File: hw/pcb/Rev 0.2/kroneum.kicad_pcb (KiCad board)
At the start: 2 copper layers, 57.6 x 68.4 mm, 18 parts, among them J1 USB_B_Micro, J2 SWD_I2C_BOOT, SW1 Boot_Mode_Btn, SW2 Ctrl_One_Btn, SW3 Reset_Btn, SW4 Ctrl_Ten_Btn, U1 STM32F042F4Px

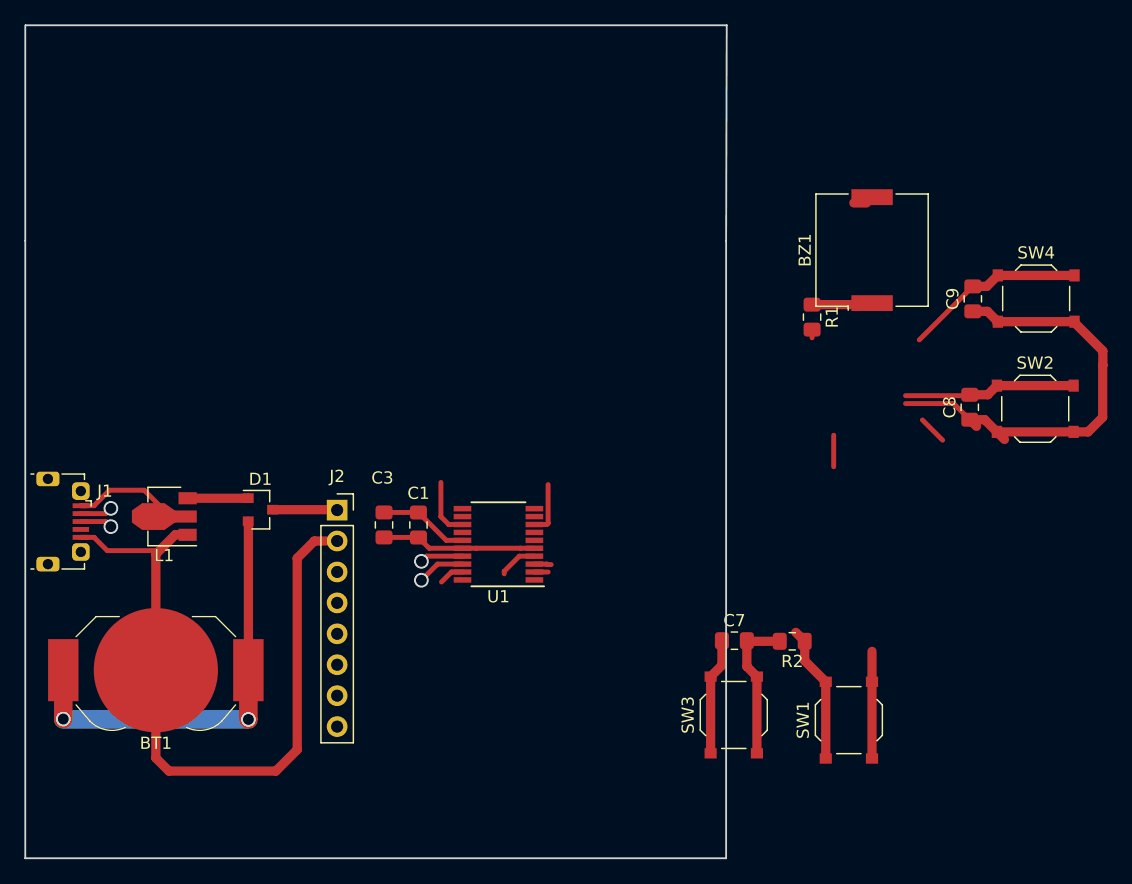
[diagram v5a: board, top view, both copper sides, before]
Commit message: hw: first PCB version with all nets connected.
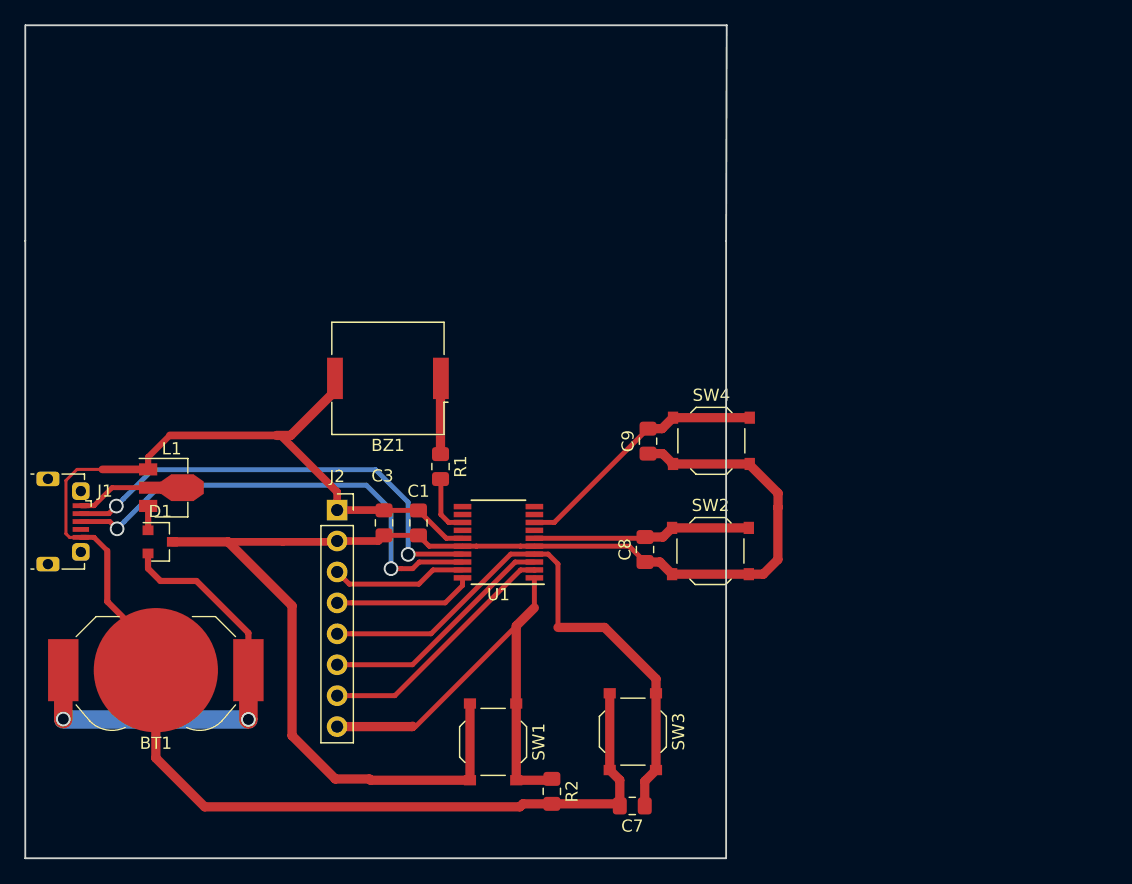
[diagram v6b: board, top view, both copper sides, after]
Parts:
- moved BZ1 41.1 mm to (151.1, 93.6), turned to 180 degrees
- moved R1 32.9 mm to (155.4, 100.8)
- moved SW1 29.3 mm to (159.8, 123.4), turned to 270 degrees
- moved SW4 29.1 mm to (177.7, 98.7)
- moved C8 29.1 mm to (172.2, 107.6)
- moved C9 29.1 mm to (172.5, 98.7)
- moved SW2 29.1 mm to (177.6, 107.8)
- moved R2 23.3 mm to (164.6, 127.5), turned to 270 degrees
- moved C7 16.0 mm to (171.2, 128.7), turned to 180 degrees
- moved D1 8.64 mm to (132.4, 107.0)
- moved SW3 8.40 mm to (171.2, 122.6), turned to 270 degrees
- moved L1 2.39 mm to (132.9, 102.6), turned to 0 degrees
- moved C1 0.17 mm to (153.6, 105.5)
- moved C3 0.17 mm to (150.8, 105.5)
- moved U1 0.17 mm to (160.2, 107.0)
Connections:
- J2 pad 1: VDD -> GND
- J2 pad 2: GND -> VDD
- J2 pad 3: SCL -> SWDIO
- J2 pad 4: SDA -> SWCLK
- J2 pad 5: BOOT0 -> NRST
- J2 pad 6: NRST -> SCL
- J2 pad 7: SWCLK -> SDA
- J2 pad 8: SWDIO -> BOOT0
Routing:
- net VDD: track 63.8 -> 114.5 mm
- net GND: track 79.6 -> 123.6 mm
- net NRST: track 13.0 -> 47.2 mm
- net USB_D+: track 6.57 -> 39.0 mm
- net USB_D-: track 6.20 -> 38.2 mm
- net BOOT0: track 11.4 -> 40.2 mm
- net SDA: track 1.27 -> 20.6 mm
- net SCL: track 3.75 -> 19.7 mm
- net SWDIO: track 2.07 -> 11.2 mm
- net SWCLK: track 2.58 -> 11.5 mm
- net Ctrl_One: track 14.1 -> 18.1 mm
- net Net-(D1-Pad1): track 4.98 -> 2.00 mm
- net Net-(BT1-Pad1): track 35.5 -> 38.0 mm
- net USB_VBUS: track 13.8 -> 11.3 mm
- net Ctrl_Ten: track 19.3 -> 21.2 mm
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
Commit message: hw: semi final PCB versions.
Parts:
- moved C7 34.0 mm to (137.2, 127.0), turned to 270 degrees
- moved SW3 29.0 mm to (142.6, 127.0), turned to 0 degrees
- moved J2 19.0 mm to (137.5, 120.9), turned to 90 degrees
- moved C8 18.8 mm to (159.0, 121.0)
- moved SW2 18.7 mm to (164.3, 121.0)
- moved R2 16.7 mm to (147.9, 127.0)
- moved C1 15.4 mm to (138.4, 107.5)
- moved C3 15.0 mm to (135.9, 107.5)
- moved C9 14.9 mm to (159.0, 105.0)
- moved SW4 14.7 mm to (164.3, 105.0)
- moved R1 14.5 mm to (141.3, 103.9), turned to 180 degrees
- moved U1 14.3 mm to (146.1, 109.2)
- moved SW1 7.42 mm to (153.2, 127.0), turned to 0 degrees
- moved BZ1 7.00 mm to (148.4, 100.1)
- moved BT1 4.77 mm to (128.7, 120.9), turned to 270 degrees
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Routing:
- net GND: track 123.6 -> 102.5 mm
- net NRST: track 47.2 -> 28.6 mm
- net USB_D-: track 38.2 -> 21.5 mm
- net USB_D+: track 39.0 -> 22.3 mm
- net BOOT0: track 40.2 -> 24.7 mm
- net VDD: track 114.5 -> 100.4 mm
- net Ctrl_One: track 18.1 -> 26.9 mm
- net Net-(BT1-Pad1): track 38.0 -> 30.2 mm, vias 2 -> 3
- net SDA: track 20.6 -> 12.9 mm
- net Net-(BZ1-Pad1): track 6.23 -> 12.6 mm
- net SCL: track 19.7 -> 13.6 mm
- net SWCLK: track 11.5 -> 15.7 mm
- net Buzzer: track 4.85 -> 6.49 mm
- net Ctrl_Ten: track 21.2 -> 20.3 mm
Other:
- board size 57.6 x 68.4 mm -> 50 x 40 mm

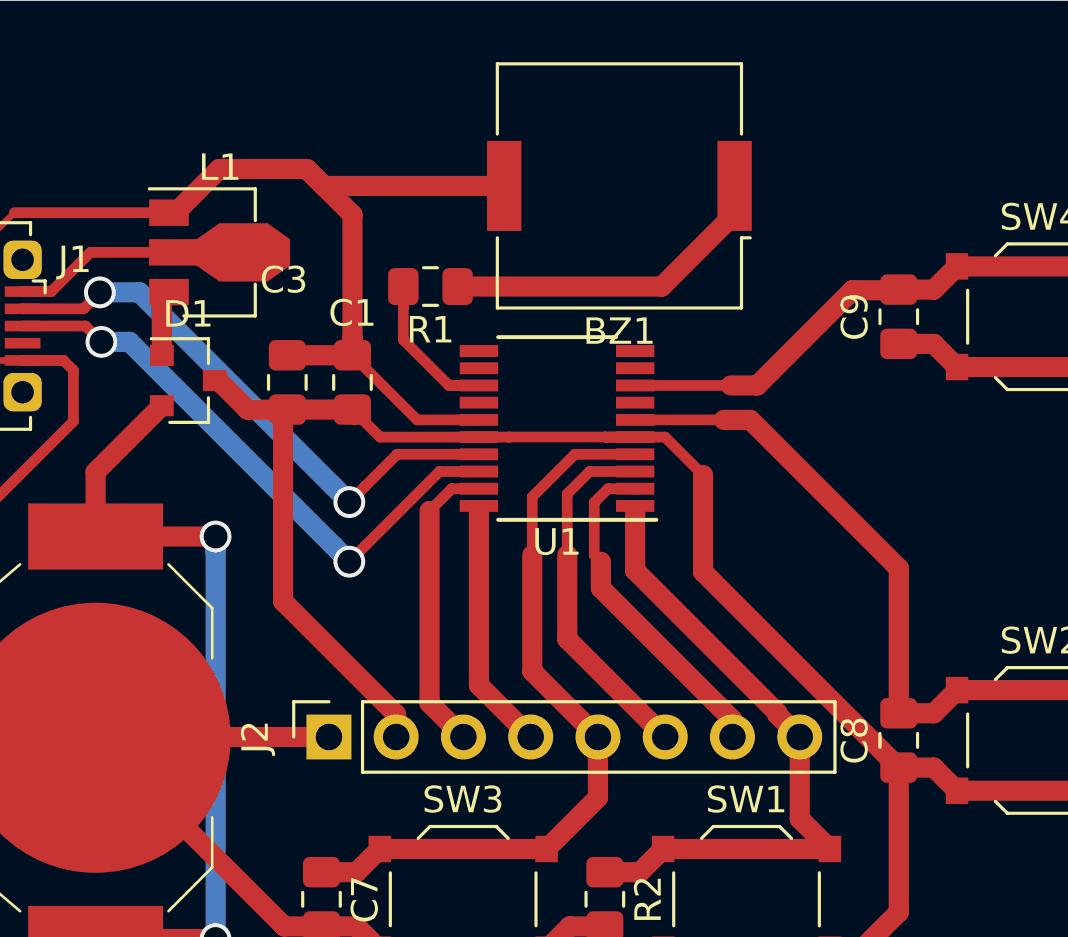
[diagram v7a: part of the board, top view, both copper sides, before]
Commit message: hw: fix PCB clearance issues.
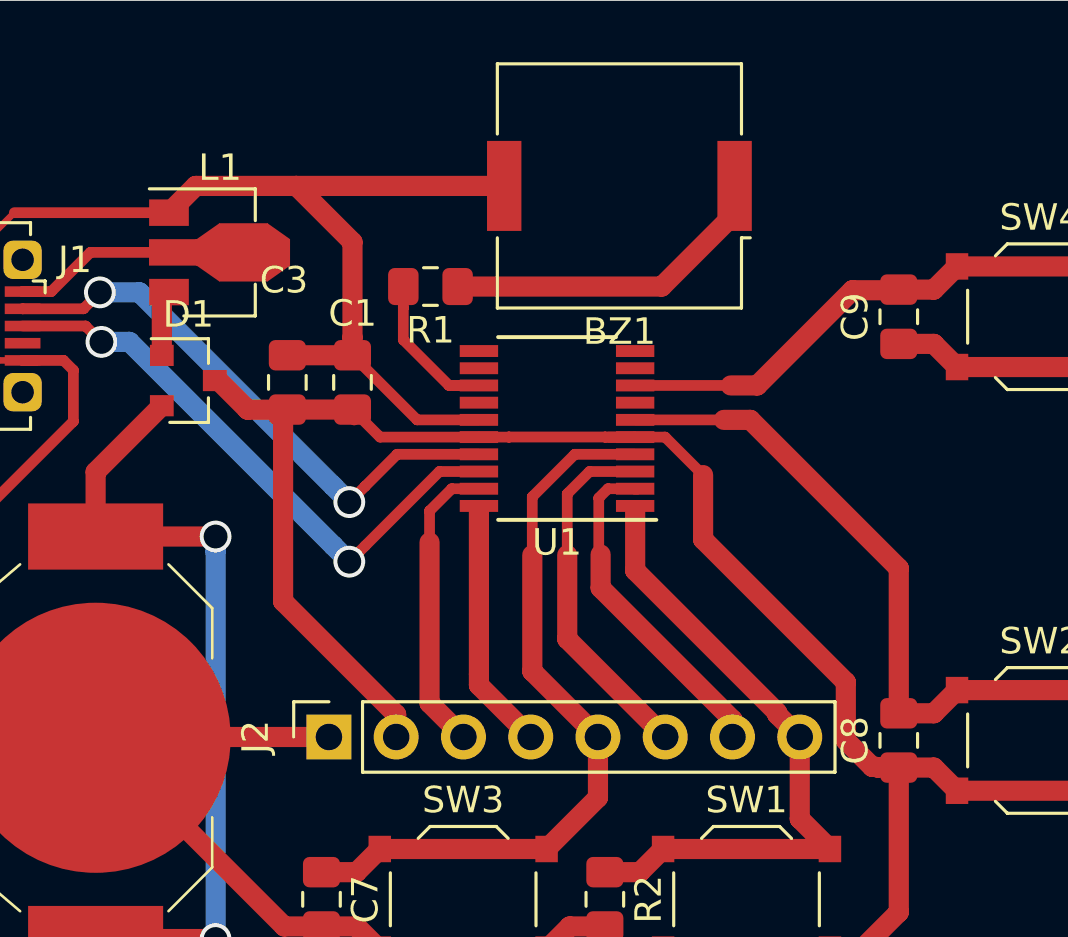
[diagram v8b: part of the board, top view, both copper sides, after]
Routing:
- net GND: track 102.5 -> 101.8 mm
- net VDD: track 100.4 -> 101.0 mm
- net Net-(BT1-Pad1): vias 3 -> 2
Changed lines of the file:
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@@
     (thickness 1.6)
     (drawings 4)
-    (tracks 183)
+    (tracks 186)
     (zones 0)
     (modules 18)
@@
   (segment (start 143.145 108.895) (end 140.81 108.895) (width 0.4064) (layer F.Cu) (net 1))
   (segment (start 138.37 105.78) (end 138.37 106.455) (width 0.762) (layer F.Cu) (net 1))
-  (segment (start 138.37 101.15) (end 138.37 105.78) (width 0.762) (layer F.Cu) (net 1))
-  (segment (start 133.34 99.42) (end 136.64 99.42) (width 0.762) (layer F.Cu) (net 1))
-  (segment (start 136.64 99.42) (end 138.37 101.15) (width 0.762) (layer F.Cu) (net 1))
   (segment (start 131.44 101.07) (end 131.69 101.07) (width 0.762) (layer F.Cu) (net 1))
-  (segment (start 131.69 101.07) (end 133.34 99.42) (width 0.762) (layer F.Cu) (net 1))
   (segment (start 147.864729 127.955) (end 148.2 127.955) (width 0.4064) (layer F.Cu) (net 1))
   (segment (start 128.7 120.87) (end 128.67 120.9) (width 0.762) (layer F.Cu) (net 1))
   (segment (start 137.48 120.87) (end 128.7 120.87) (width 0.762) (layer F.Cu) (net 1))
-  (segment (start 137.28 100.06) (end 144.1 100.06) (width 0.762) (layer F.Cu) (net 1))
-  (segment (start 136.64 99.42) (end 137.28 100.06) (width 0.762) (layer F.Cu) (net 1))
   (segment (start 126.88 120.9) (end 123.180001 117.200001) (width 0.762) (layer F.Cu) (net 1))
   (segment (start 128.67 120.9) (end 126.88 120.9) (width 0.762) (layer F.Cu) (net 1))
@@
   (segment (start 128.67 120.9) (end 135.795 128.025) (width 0.762) (layer F.Cu) (net 1))
   (segment (start 135.91 106.455) (end 138.37 106.455) (width 0.762) (layer F.Cu) (net 1))
+  (segment (start 132.45 100.06) (end 131.44 101.07) (width 0.762) (layer F.Cu) (net 1))
+  (segment (start 138.37 102.18) (end 138.37 105.78) (width 0.762) (layer F.Cu) (net 1))
+  (segment (start 136.25 100.06) (end 138.37 102.18) (width 0.762) (layer F.Cu) (net 1))
+  (segment (start 144.1 100.06) (end 136.25 100.06) (width 0.762) (layer F.Cu) (net 1))
+  (segment (start 136.25 100.06) (end 132.45 100.06) (width 0.762) (layer F.Cu) (net 1))
   (segment (start 152.8 101.11) (end 152.8 100.06) (width 0.762) (layer F.Cu) (net 2))
   (segment (start 150.05 103.86) (end 152.8 101.11) (width 0.762) (layer F.Cu) (net 2))
@@
   (segment (start 159 122.025) (end 160.325 122.025) (width 0.762) (layer F.Cu) (net 3))
   (segment (start 161.2 122.9) (end 167.5 122.9) (width 0.762) (layer F.Cu) (net 3))
-  (segment (start 151.610789 110.979389) (end 151.610789 114.635789) (width 0.762) (layer F.Cu) (net 3))
-  (segment (start 151.610789 114.635789) (end 159 122.025) (width 0.762) (layer F.Cu) (net 3))
   (segment (start 140.02 120.02) (end 140.02 120.87) (width 0.762) (layer F.Cu) (net 3))
   (segment (start 135.75 115.75) (end 140.02 120.02) (width 0.762) (layer F.Cu) (net 3))
@@
   (segment (start 159 122.025) (end 159 127.487) (width 0.762) (layer F.Cu) (net 3))
   (segment (start 156.4 128.9) (end 150.1 128.9) (width 0.762) (layer F.Cu) (net 3))
+  (segment (start 151.610789 113.410789) (end 151.610789 110.979389) (width 0.762) (layer F.Cu) (net 3))
+  (segment (start 158.2 122.025) (end 158.175 122) (width 0.762) (layer F.Cu) (net 3))
+  (segment (start 157 121) (end 157 118.8) (width 0.762) (layer F.Cu) (net 3))
+  (segment (start 159 122.025) (end 158.2 122.025) (width 0.762) (layer F.Cu) (net 3))
+  (segment (start 158 122) (end 157 121) (width 0.762) (layer F.Cu) (net 3))
+  (segment (start 157 118.8) (end 151.610789 113.410789) (width 0.762) (layer F.Cu) (net 3))
+  (segment (start 158.175 122) (end 158 122) (width 0.762) (layer F.Cu) (net 3))
   (segment (start 159 119.975) (end 159.275 119.975) (width 0.4064) (layer F.Cu) (net 4))
   (segment (start 149.045 108.895) (end 152.395 108.895) (width 0.4064) (layer F.Cu) (net 4))
@@
   (segment (start 128.67 113.3) (end 128.67 110.86) (width 0.762) (layer F.Cu) (net 15))
   (segment (start 128.67 113.3) (end 133.2 113.3) (width 0.762) (layer F.Cu) (net 15))
-  (via (at 133.2 113.3) (size 0.8) (drill 0.4) (layers F.Cu B.Cu) (net 15))
   (segment (start 133.2 113.3) (end 133.2 113.3) (width 0.762) (layer F.Cu) (net 15))
   (via (at 133.2 113.3) (size 1.2) (drill 0.9) (layers F.Cu B.Cu) (net 15))
@@
   (segment (start 142.119238 111.495) (end 141.28 112.334238) (width 0.4064) (layer F.Cu) (net 20))
   (segment (start 141.28 119.59) (end 142.56 120.87) (width 0.762) (layer F.Cu) (net 20))
-  (segment (start 141.28 112.334238) (end 141.28 119.59) (width 0.762) (layer F.Cu) (net 20))
+  (segment (start 141.28 112.334238) (end 141.28 113.52) (width 0.4064) (layer F.Cu) (net 20))
+  (segment (start 141.28 113.52) (end 141.28 119.59) (width 0.762) (layer F.Cu) (net 20))
   (segment (start 143.145 118.915) (end 143.145 118.5) (width 0.762) (layer F.Cu) (net 21))
   (segment (start 145.1 120.87) (end 143.145 118.915) (width 0.762) (layer F.Cu) (net 21))
@@
   (segment (start 149.045 111.495) (end 149.045 111.516799) (width 0.4064) (layer F.Cu) (net 22))
   (segment (start 152.72 120.22) (end 152.72 120.87) (width 0.762) (layer F.Cu) (net 22))
-  (segment (start 147.75 114.25) (end 147.75 115.25) (width 0.762) (layer F.Cu) (net 22))
-  (segment (start 147.75 115.25) (end 152.72 120.22) (width 0.762) (layer F.Cu) (net 22))
-  (segment (start 147.5 114) (end 147.75 114.25) (width 0.4064) (layer F.Cu) (net 22))
-  (segment (start 147.5 112.014238) (end 147.5 114) (width 0.4064) (layer F.Cu) (net 22))
+  (segment (start 147.74 113.98) (end 147.74 115.24) (width 0.762) (layer F.Cu) (net 22))
+  (segment (start 147.74 115.24) (end 152.72 120.22) (width 0.762) (layer F.Cu) (net 22))
+  (segment (start 147.67 111.844238) (end 147.67 113.83) (width 0.4064) (layer F.Cu) (net 22))
   (segment (start 149.045 111.495) (end 148.019238 111.495) (width 0.4064) (layer F.Cu) (net 22))
-  (segment (start 148.019238 111.495) (end 147.5 112.014238) (width 0.4064) (layer F.Cu) (net 22))
+  (segment (start 148.019238 111.495) (end 147.67 111.844238) (width 0.4064) (layer F.Cu) (net 22))
   (segment (start 149.045 110.845) (end 147.325 110.845) (width 0.4064) (layer F.Cu) (net 23))
   (segment (start 147.325 110.845) (end 146.48 111.69) (width 0.4064) (layer F.Cu) (net 23))
